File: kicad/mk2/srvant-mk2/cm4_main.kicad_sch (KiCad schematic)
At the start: 69 parts, among them J10 HDMI connector, J11 USB A, J6 Conn_02x05_Odd_Even, J8 Bus_M.2_Socket_M, J9 ARJM11, U13 74AHC1G04, U14 AP22653W6, U16 FSUSB42MUX, U17 PCF85063AT/AAZ, U18 74LVC1G07SE-7, U19 TPD4EUSB30, U20 TPD4EUSB30, U21 74LVC1G07SE-7, U23 SLB9670VQ20FW785XTMA1, U24 74AHC1G08, Y3 X32K768S301

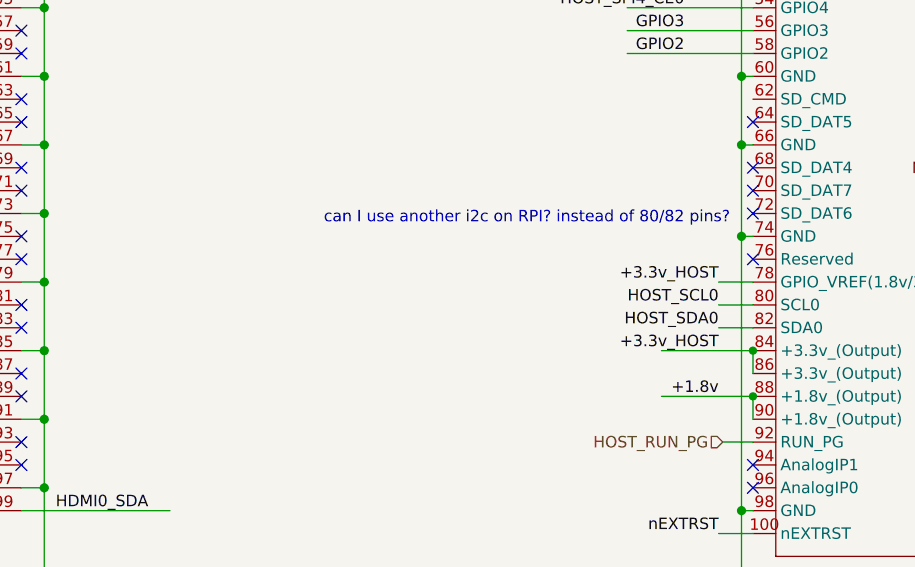
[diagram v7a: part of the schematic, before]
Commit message: small fixes
* fix unconnected vias near M2
* fix missing resistors near rpi i2c
* silkscreen fixes
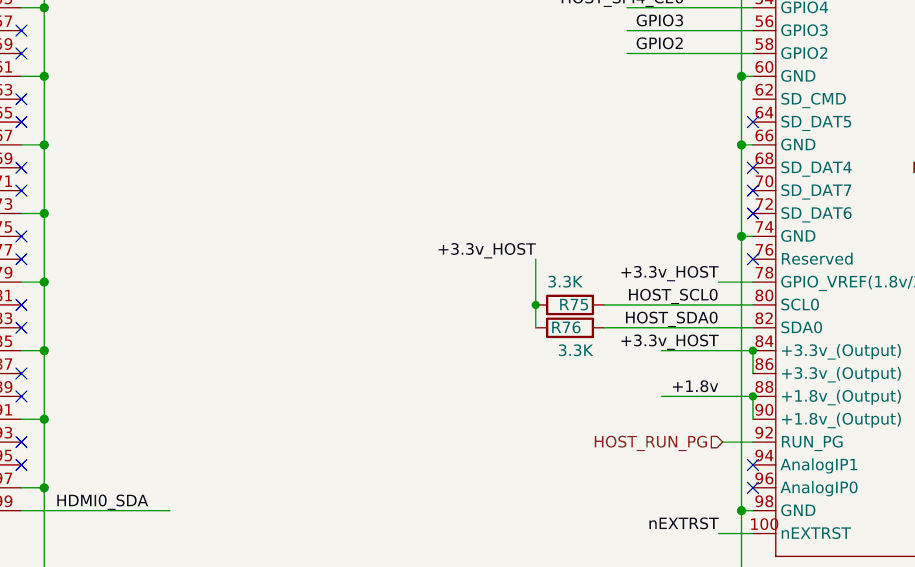
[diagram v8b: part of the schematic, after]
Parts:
- added R75, R76: 3.3K, Resistor_SMD:R_0402_1005Metric, symbol Device:R
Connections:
- net +3.3v_HOST: now also R75.2, R76.1
- net HOST_SCL0: now also R75.1
- net HOST_SDA0: now also R76.2
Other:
- note removed: "can I use another i2c on RPI? instead of 80/82 pins?"
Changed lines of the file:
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@@
   (junction (at 109.22 132.08) (diameter 1.016) (color 0 0 0 0)
   )
+  (junction (at 162.56 358.14) (diameter 0) (color 0 0 0 0)
+  )
   (junction (at 41.91 332.74) (diameter 1.016) (color 0 0 0 0)
   )
@@
     (stroke (width 0) (type solid))
   )
+  (wire (pts (xy 162.56 358.14) (xy 162.56 360.68))
+    (stroke (width 0) (type default))
+  )
   (wire (pts (xy 492.76 208.28) (xy 492.76 212.09))
     (stroke (width 0) (type default))
@@
     (stroke (width 0) (type solid))
   )
+  (wire (pts (xy 162.56 353.06) (xy 162.56 358.14))
+    (stroke (width 0) (type default))
+  )
   (wire (pts (xy 559.054 359.918) (xy 566.42 359.918))
     (stroke (width 0) (type solid))
@@
     (stroke (width 0) (type solid))
   )
-  (wire (pts (xy 182.88 360.68) (xy 186.69 360.68))
+  (wire (pts (xy 170.18 360.68) (xy 186.69 360.68))
     (stroke (width 0) (type solid))
   )
@@
     (stroke (width 0) (type solid))
   )
-  (wire (pts (xy 182.88 358.14) (xy 186.69 358.14))
+  (wire (pts (xy 170.18 358.14) (xy 186.69 358.14))
     (stroke (width 0) (type solid))
   )
@@
     (effects (font (size 1.27 1.27)) (justify left bottom))
   )
-  (text "can I use another i2c on RPI? instead of 80/82 pins?"
-    (at 184.15 349.25 0)
-    (effects (font (size 1.27 1.27)) (justify right bottom))
-  )
   (text "PWR LED" (at 454.66 365.76 0)
     (effects (font (size 1.27 1.27)) (justify left bottom))
@@
     )
   )
+  (label "+3.3v_HOST" (at 162.56 353.06 180) (fields_autoplaced)
+    (effects (font (size 1.27 1.27)) (justify right bottom))
+  )
   (label "USB2_P" (at 175.26 152.4 180) (fields_autoplaced)
     (effects (font (size 1.27 1.27)) (justify right bottom))
@@
     )
   )
+  (symbol (lib_id "Device:R") (at 166.37 360.68 90) (unit 1)
+    (in_bom yes) (on_board yes) (dnp no)
+    (property "Reference" "R76" (at 167.64 360.68 90)
+      (effects (font (size 1.27 1.27)) (justify left))
+    )
+    (property "Value" "3.3K" (at 168.91 363.22 90)
+      (effects (font (size 1.27 1.27)) (justify left))
+    )
+    (property "Footprint" "Resistor_SMD:R_0402_1005Metric" (at 166.37 362.458 90)
+      (effects (font (size 1.27 1.27)) hide)
+    )
+    (property "Datasheet" "~" (at 166.37 360.68 0)
+      (effects (font (size 1.27 1.27)) hide)
+    )
+    (property "manf#" "" (at 166.37 360.68 0)
+      (effects (font (size 1.27 1.27)) hide)
+    )
+    (property "digikey#" "" (at 166.37 360.68 0)
+      (effects (font (size 1.27 1.27)) hide)
+    )
+    (property "mouser#" "" (at 166.37 360.68 0)
+      (effects (font (size 1.27 1.27)) hide)
+    )
+    (property "farnell#" "" (at 166.37 360.68 0)
+      (effects (font (size 1.27 1.27)) hide)
+    )
+    (property "rs#" "" (at 166.37 360.68 0)
+      (effects (font (size 1.27 1.27)) hide)
+    )
+    (property "Part Description" "" (at 166.37 360.68 0)
+      (effects (font (size 1.27 1.27)) hide)
+    )
+    (pin "1")
+    (pin "2")
+    (instances
+      (project "srvant-mk2"
+        (path "/1859a578-b791-4142-bdf4-fda494df1146/75d0860a-7ab5-4d7d-b96d-9266ebc33987"
+          (reference "R76") (unit 1)
+        )
+      )
+    )
+  )
   (symbol (lib_id "Mechanical:MountingHole") (at 512.445 357.124 0) (unit 1)
     (in_bom yes) (on_board yes) (dnp no)
@@
         )
       )
+    )
+  )
+  (symbol (lib_id "Device:R") (at 166.37 358.14 270) (mirror x) (unit 1)
+    (in_bom yes) (on_board yes) (dnp no)
+    (property "Reference" "R75" (at 165.1 358.14 90)
+      (effects (font (size 1.27 1.27)) (justify left))
+    )
+    (property "Value" "3.3K" (at 163.83 355.6 90)
+      (effects (font (size 1.27 1.27)) (justify left))
+    )
+    (property "Footprint" "Resistor_SMD:R_0402_1005Metric" (at 166.37 359.918 90)
+      (effects (font (size 1.27 1.27)) hide)
+    )
+    (property "Datasheet" "~" (at 166.37 358.14 0)
+      (effects (font (size 1.27 1.27)) hide)
+    )
+    (property "manf#" "" (at 166.37 358.14 0)
+      (effects (font (size 1.27 1.27)) hide)
+    )
+    (property "digikey#" "" (at 166.37 358.14 0)
+      (effects (font (size 1.27 1.27)) hide)
+    )
+    (property "mouser#" "" (at 166.37 358.14 0)
+      (effects (font (size 1.27 1.27)) hide)
+    )
+    (property "farnell#" "" (at 166.37 358.14 0)
+      (effects (font (size 1.27 1.27)) hide)
+    )
+    (property "rs#" "" (at 166.37 358.14 0)
+      (effects (font (size 1.27 1.27)) hide)
+    )
+    (property "Part Description" "" (at 166.37 358.14 0)
+      (effects (font (size 1.27 1.27)) hide)
+    )
+    (pin "1")
+    (pin "2")
+    (instances
+      (project "srvant-mk2"
+        (path "/1859a578-b791-4142-bdf4-fda494df1146/75d0860a-7ab5-4d7d-b96d-9266ebc33987"
+          (reference "R75") (unit 1)
+        )
+      )
